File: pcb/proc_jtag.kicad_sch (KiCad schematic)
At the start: 17 parts, among them SW1 SW_Push, U1 XC6SLX16-FTG256, U11 74LVC1G08, U15 BCM56DS, U16 74LS32, U17 74LS04, U18 74LS08, U19 NE555P

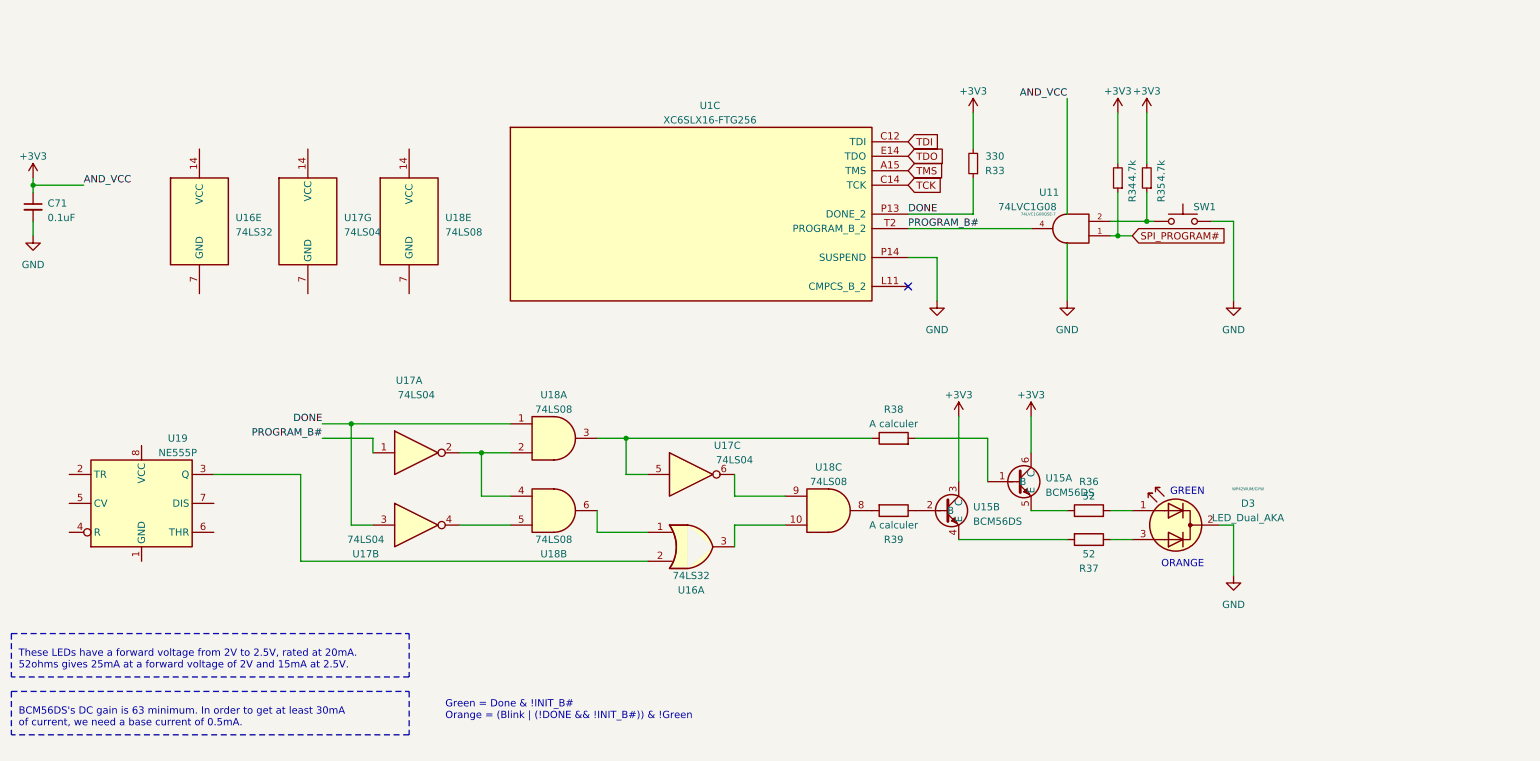
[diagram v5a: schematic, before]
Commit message: add the led blinking logic
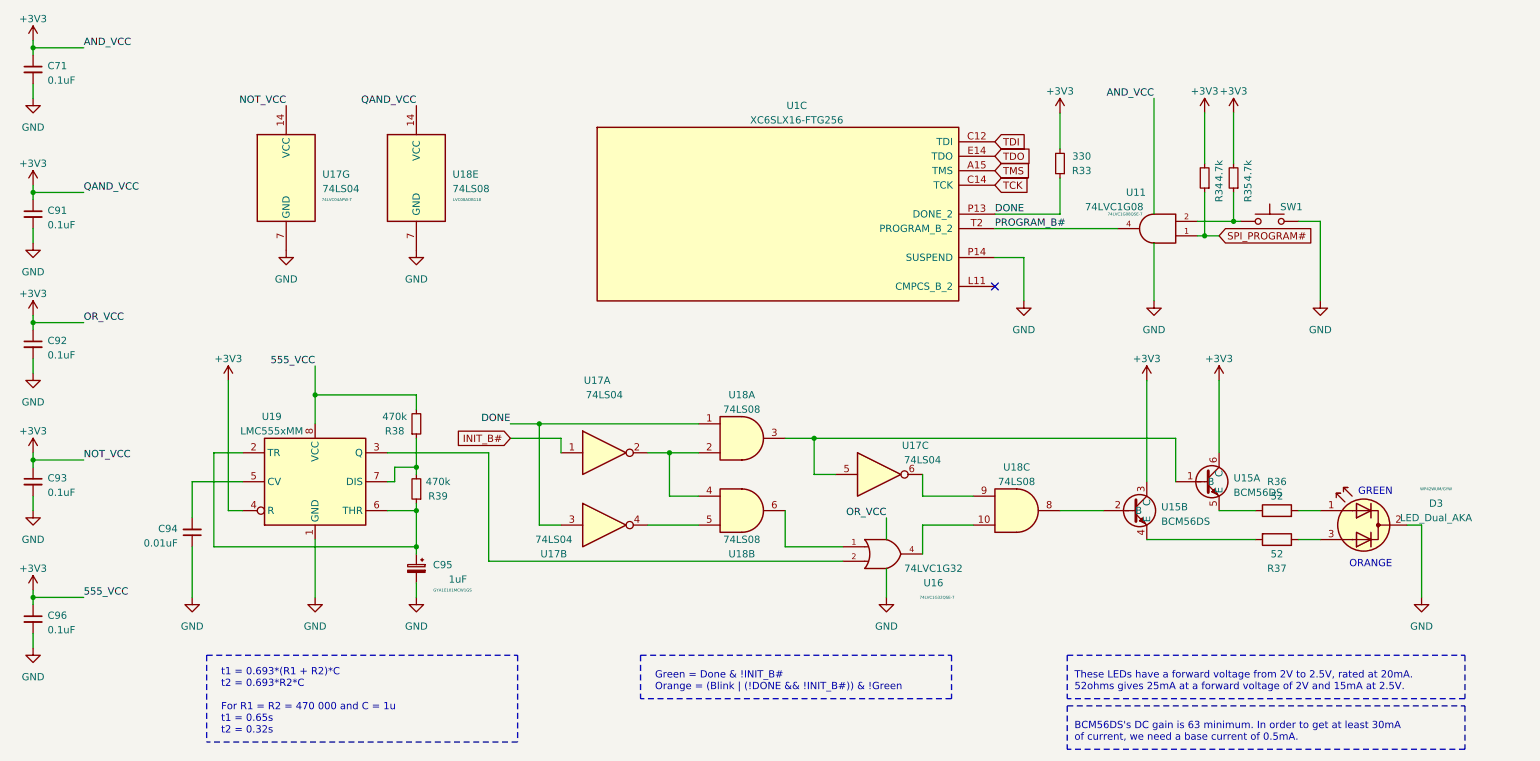
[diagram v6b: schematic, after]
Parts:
- removed R38, R39: A calculer, symbol Device:R
- removed U16: 74LS32, symbol 74xx:74LS32
- removed U19: NE555P, symbol Timer:NE555P
- added C91, C92, C93, C96: 0.1uF, Capacitor_SMD:C_0402_1005Metric, symbol Device:C_Small
- added C94: 0.01uF, Capacitor_SMD:C_0402_1005Metric, symbol Device:C_Small
- added C95: 1uF, Capacitor_SMD:CP_Elec_6.3x7.7, symbol Device:C_Polarized_Small
- added R38, R39: 470k, Resistor_SMD:R_0402_1005Metric, symbol Device:R_Small
- added U16: 74LVC1G32, Package_TO_SOT_SMD:SOT-353_SC-70-5, symbol 74xGxx:74LVC1G32
- added U19: LMC555xMM, Package_SO:VSSOP-8_3.0x3.0mm_P0.65mm, symbol Timer:LMC555xMM
- D3: footprint (none) -> LED_THT:WP42WUM,GYW
- R36, R37: footprint (none) -> Resistor_SMD:R_0402_1005Metric
- U15: footprint (none) -> Package_SO:TSOP-6_1.65x3.05mm_P0.95mm
- U17: footprint (none) -> Package_SO:TSSOP-14_4.4x5mm_P0.65mm; Ref (none) -> 74LVC04APW-T
- U17: footprint (none) -> Package_SO:TSSOP-14_4.4x5mm_P0.65mm
- U18: footprint (none) -> Package_SO:SSOP-14_5.3x6.2mm_P0.65mm
- U18: footprint (none) -> Package_SO:SSOP-14_5.3x6.2mm_P0.65mm; Ref (none) -> LVC08ADB118
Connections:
- net +3V3: now also U17.14 (VCC), U17.7 (GND), U18.14 (VCC), U18.7 (GND), C91.1, C91.2, C92.1, C92.2, C93.1, C93.2, C94.1, C95.2, C96.1, C96.2, R38.2, U16.3 (GND), U16.5 (VCC), U19.1 (GND), U19.4 (R), U19.8 (VCC)
- net PROGRAM_B#: no longer U17.1
- net at U18.10: now also U16.4
- net at U18.8: now also U15.2 (B)
- net at U18.6: now also U16.1
- net at U15.1 (B): now also U17.5, U18.3
- new net: C95.1, R39.1, U19.2 (TR), U19.6 (THR)
- new net: U16.2, U19.3 (Q)
- new net: C94.2, U19.5 (CV)
- new net: R38.1, R39.2, U19.7 (DIS)
- new net INIT_B#: U17.1
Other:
- note added: "t1 = 0.693*(R1 + R2)*C t2 = 0.693*R2*C For R1 = R2 = 470 000 and C = 1u t1 = 0.65s t2 = 0.32s"
- moved on the sheet: C71, D3, R33, R34, R35, R36, R37, SW1, U11, U15A, U15B, U17A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

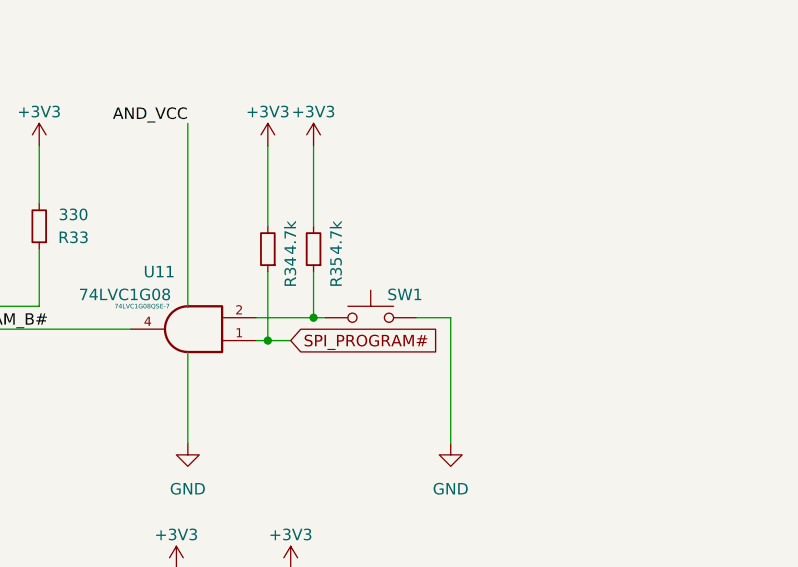
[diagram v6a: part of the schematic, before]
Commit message: add footprint for the button
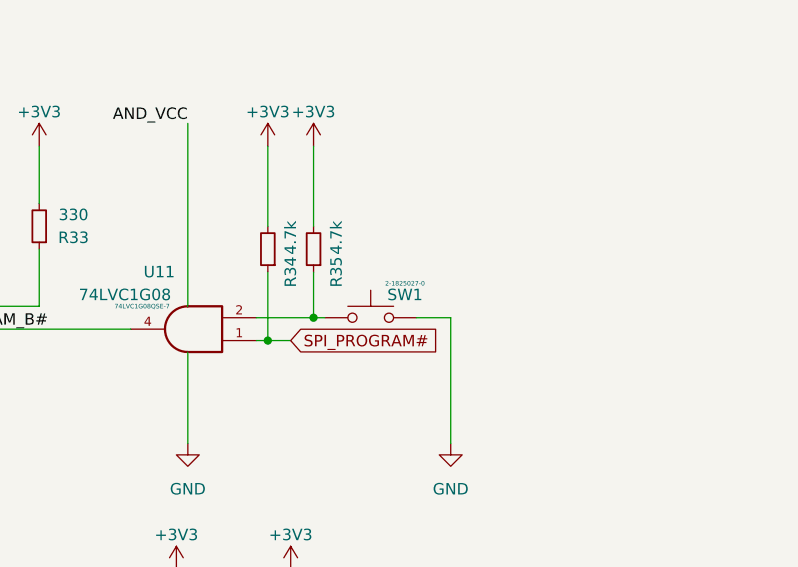
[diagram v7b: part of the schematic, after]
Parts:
- SW1: footprint (none) -> Button_Switch_THT:2-1825027-0; Ref (none) -> 2-1825027-0
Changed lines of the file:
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@@
       (effects (font (size 1.27 1.27)) hide)
     )
-    (property "Footprint" "" (id 2) (at 241.3 49.53 0)
+    (property "Footprint" "Button_Switch_THT:2-1825027-0" (id 2) (at 241.3 49.53 0)
       (effects (font (size 1.27 1.27)) hide)
     )
@@
       (effects (font (size 1.27 1.27)) hide)
     )
+    (property "Ref" "2-1825027-0 " (id 4) (at 245.11 50.8 0)
+      (effects (font (size 0.5 0.5)))
+    )
     (pin "1")

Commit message: add components to pcb
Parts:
- D3: footprint LED_THT:WP42WUM,GYW -> WP42WUMGYW:WP42WUM,GYW
- SW1: footprint Button_Switch_THT:2-1825027-0 -> 2-1825027-0:2-1825027-0
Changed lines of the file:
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@@
-(kicad_sch (version 20210126) (generator eeschema)
+(kicad_sch (version 20210406) (generator eeschema)
   (paper "User" 299.999 180.01)
   (junction (at 24.13 24.13) (diameter 0.9144) (color 0 0 0 0))
@@
       (effects (font (size 1.27 1.27)) hide)
     )
-    (property "Footprint" "Button_Switch_THT:2-1825027-0" (id 2) (at 241.3 49.53 0)
+    (property "Footprint" "2-1825027-0:2-1825027-0" (id 2) (at 241.3 49.53 0)
       (effects (font (size 1.27 1.27)) hide)
     )
@@
     (property "Reference" "D3" (id 0) (at 270.51 104.14 0))
     (property "Value" "LED_Dual_AKA" (id 1) (at 270.51 106.68 0))
-    (property "Footprint" "LED_THT:WP42WUM,GYW" (id 2) (at 257.81 107.95 0)
-      (effects (font (size 1.27 1.27)) hide)
-    )
+    (property "Footprint" "WP42WUMGYW:WP42WUM,GYW" (id 2) (at 257.81 107.95 0)
+      (effects (font (size 1.27 1.27)) hide)
+    )
